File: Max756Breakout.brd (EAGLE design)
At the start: 26.6 x 26.6 mm, 11 parts

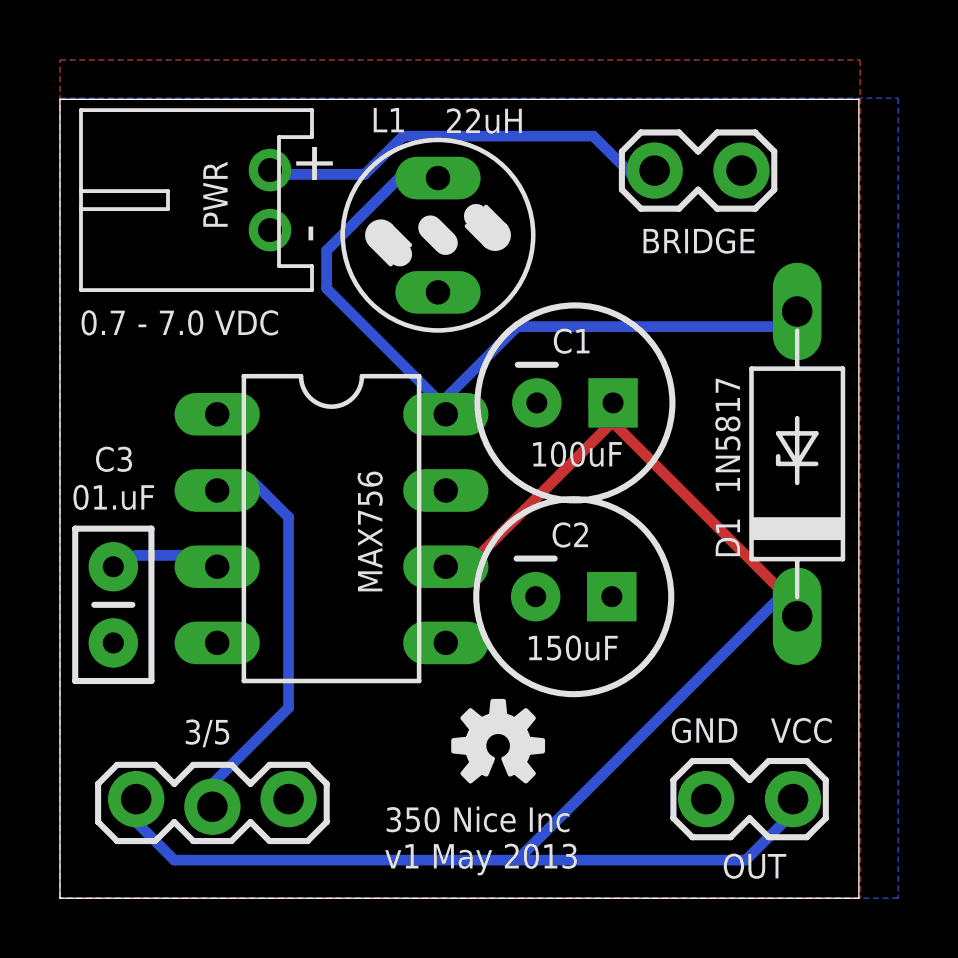
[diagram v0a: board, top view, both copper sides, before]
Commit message: Added LED for v2
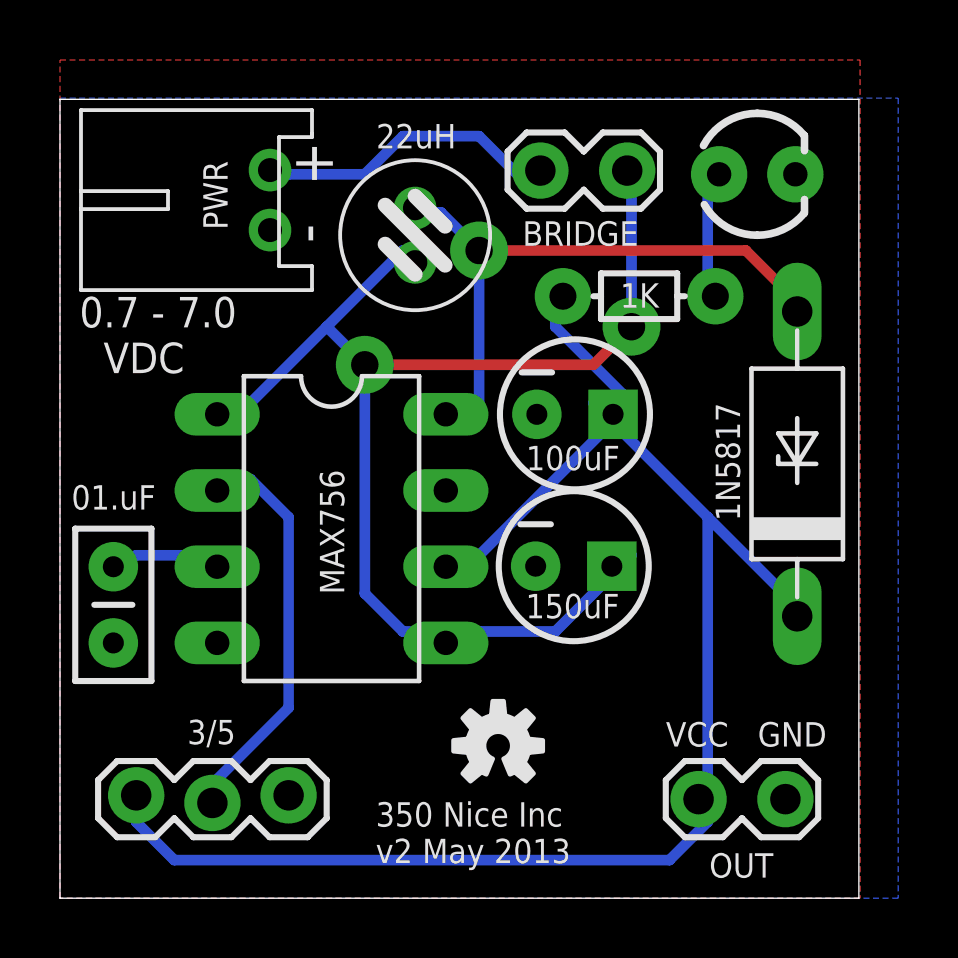
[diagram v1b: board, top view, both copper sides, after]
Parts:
- added LED1: (no value), Dek:LED3MM
- added R1: 1K, Dek:AXIAL-0.2
- C1, C2: device SparkFun-Capacitors:CPOL-RADIAL-100UF-25V -> SparkFun-Capacitors:CPOL-RADIAL-10UF-25V
- moved BRIDGE 3.81 mm to (18.7, 24.3)
- moved OUT 2.79 mm to (21.5, 3.30), turned to 0 degrees
- moved C2 1.02 mm to (17.1, 11.1)
- moved L1 0.76 mm to (11.8, 22.1)
- moved C1 0.38 mm to (17.2, 16.1)
- moved 3/5 0.13 mm to (2.54, 3.30)
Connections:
- new net N$2: LED1.A, R1.P$2
- net GND: now also LED1.K
- net VCC: now also R1.P$1
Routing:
- net VIN: track 0.00 -> 44.6 mm, vias 0 -> 2
- net N$2: track 0.00 -> 4.55 mm
- net N$1: track 13.9 -> 10.1 mm
- net L1: track 25.0 -> 21.3 mm, vias 0 -> 1
- net VCC: track 57.2 -> 56.2 mm
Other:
- board text added: "350 Nice Inc v2 May 2013"
- board text removed: "350 Nice Inc v1 May 2013"

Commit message: Exported PDF schematic
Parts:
- added FRAME1: FRAME-LETTER, SparkFun-Aesthetics:CREATIVE_COMMONS
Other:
- board text added: "Max756 Breakout v2 May 2013"
- board text removed: "350 Nice Inc v2 May 2013"
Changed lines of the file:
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@@
 <layer number="23" name="tOrigins" color="15" fill="1" visible="yes" active="yes"/>
 <layer number="24" name="bOrigins" color="15" fill="1" visible="yes" active="yes"/>
-<layer number="25" name="tNames" color="16" fill="1" visible="yes" active="yes"/>
+<layer number="25" name="tNames" color="16" fill="1" visible="no" active="yes"/>
 <layer number="26" name="bNames" color="7" fill="1" visible="no" active="yes"/>
 <layer number="27" name="tValues" color="7" fill="1" visible="no" active="yes"/>
@@
 <text x="0.651" y="17.502" size="1.016" layer="21" font="vector" ratio="15">0.7 - 7.0
   VDC</text>
-<text x="10.525" y="1.167" size="0.8128" layer="21" font="vector" ratio="15">350 Nice Inc
+<text x="9.255" y="1.167" size="0.8128" layer="21" font="vector" ratio="15">Max756 Breakout
 v2 May 2013</text>
 <rectangle x1="3.683" y1="15.367" x2="6.731" y2="17.018" layer="41"/>
@@
 </element>
 <element name="U$1" library="SparkFun-Aesthetics" package="OSHW-LOGO-S" value="" x="14.605" y="5.08"/>
+<element name="FRAME1" library="SparkFun-Aesthetics" package="CREATIVE_COMMONS" value="FRAME-LETTER" x="21.59" y="-7.62"/>
 </elements>
 <signals>
